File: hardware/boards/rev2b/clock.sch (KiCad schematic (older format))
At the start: 21 parts, among them U1 LP5907MFX-3.3, U2 LP5907MFX-1.8, U3 KT2520K-T, U4 NC7SVU04P5X, U5 NB3N551

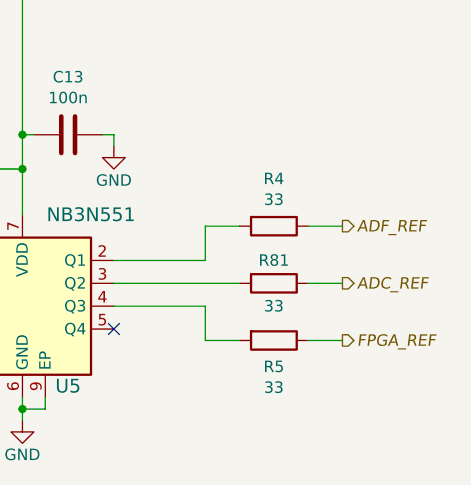
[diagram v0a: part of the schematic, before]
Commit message: rev2 pcb: finish routing traces
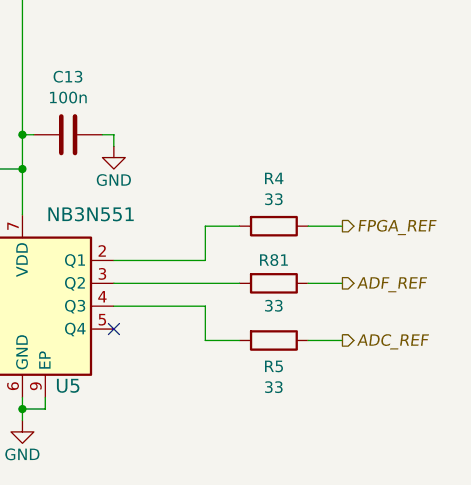
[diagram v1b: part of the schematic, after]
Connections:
- net ADC_REF: now also R5.1; no longer R81.1
- net ADF_REF: now also R81.1; no longer R4.1
- net FPGA_REF: now also R4.1; no longer R5.1
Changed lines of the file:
@@
 Text HLabel 5600 2050 0    50   Input Italic 0
 3V6
+Text HLabel 10100 4150 2    50   Output Italic 0
+FPGA_REF
+Text HLabel 10100 4400 2    50   Output Italic 0
+ADF_REF
 Text HLabel 10100 4650 2    50   Output Italic 0
-FPGA_REF
-Text HLabel 10100 4150 2    50   Output Italic 0
-ADF_REF
-Text HLabel 10100 4400 2    50   Output Italic 0
 ADC_REF
 $Comp
